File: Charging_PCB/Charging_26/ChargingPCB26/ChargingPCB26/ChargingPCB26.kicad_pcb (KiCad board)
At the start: 2 copper layers, 100 x 100 mm, 61 parts, among them J1 Molex6pin, J2 Molex6pin, K101 Relay_SPDT_Omron_G2RL-1, K102 Relay_SPDT_Omron_G2RL-1, Q1 Q_NMOS_GDS, Q103 Q_NPN_BEC, Q104 Q_NPN_BEC, Q105 Q_NPN_BEC, Q106 Q_NPN_BEC, Q2 Q_NMOS_GDS, Q3 Q_NMOS_GDS, Q4 Q_NMOS_GDS, SW101 SW_Omron_B3FS, SW102 SW_Omron_B3FS, U1 SFH617A-1, U107 LM7805_TO220, U2 SFH617A-1, U5 74LS279, U6 74HC00

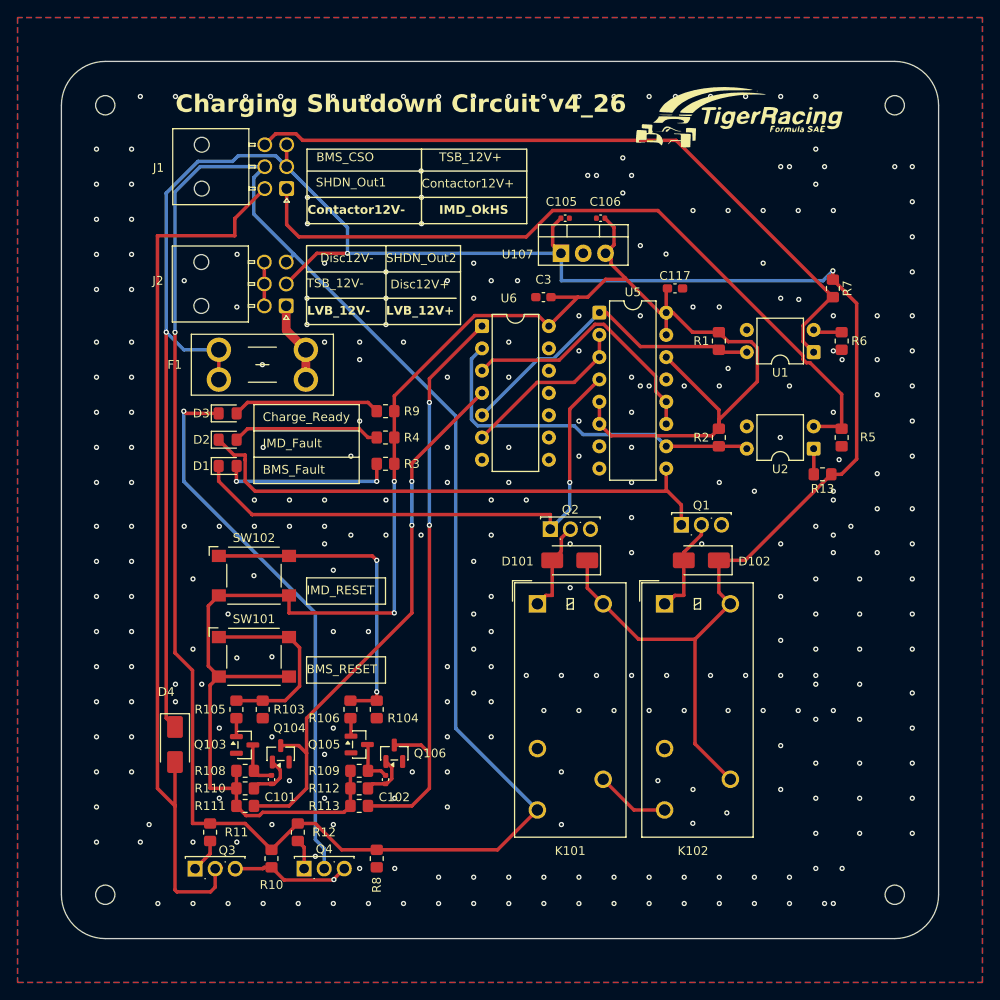
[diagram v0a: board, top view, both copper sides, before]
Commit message: Charging PCB 12V+ wire length increased
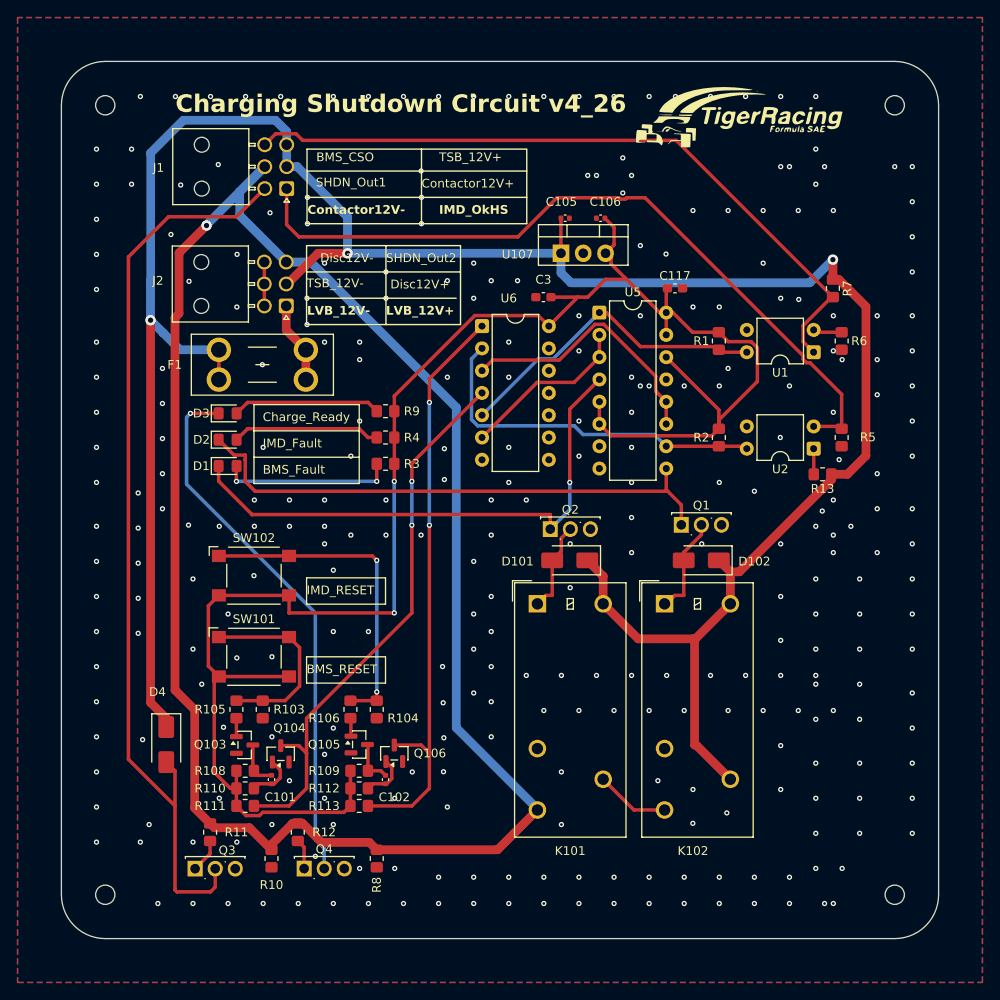
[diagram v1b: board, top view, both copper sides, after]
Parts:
- moved D4 1.00 mm to (62.0, 127.9)
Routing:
- net GND: track 18.6 -> 5.00 mm, vias 314 -> 308
- net +12V: track 264.6 -> 278.1 mm
- net /Charger_SHDN: track 217.7 -> 214.3 mm
- net /-12V_Contactor: track 103.4 -> 105.9 mm
- net +5V: track 210.0 -> 208.3 mm
- net /IMD_OKhs: track 85.4 -> 86.7 mm
- net Net-(D3-K): track 63.2 -> 62.1 mm
